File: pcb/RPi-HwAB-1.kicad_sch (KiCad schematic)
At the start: 5 parts, among them U1 CAT24C256

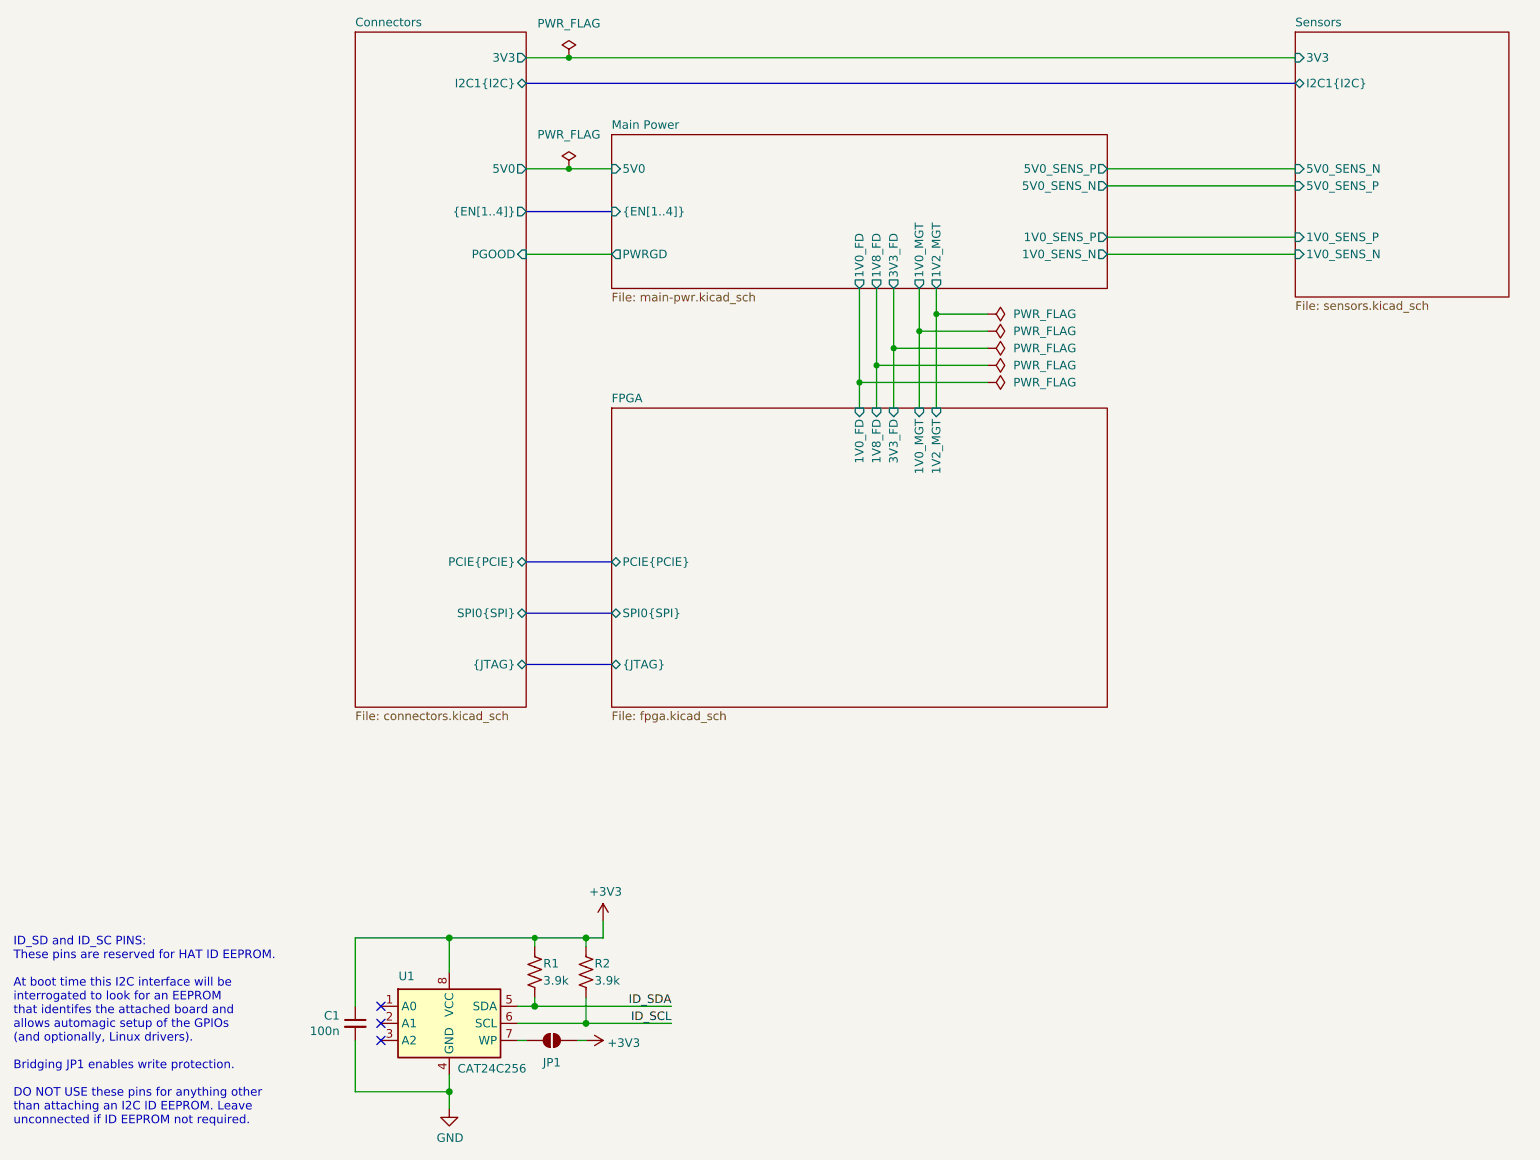
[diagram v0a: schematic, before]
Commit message: added dram, defined pcie sideband sigs.
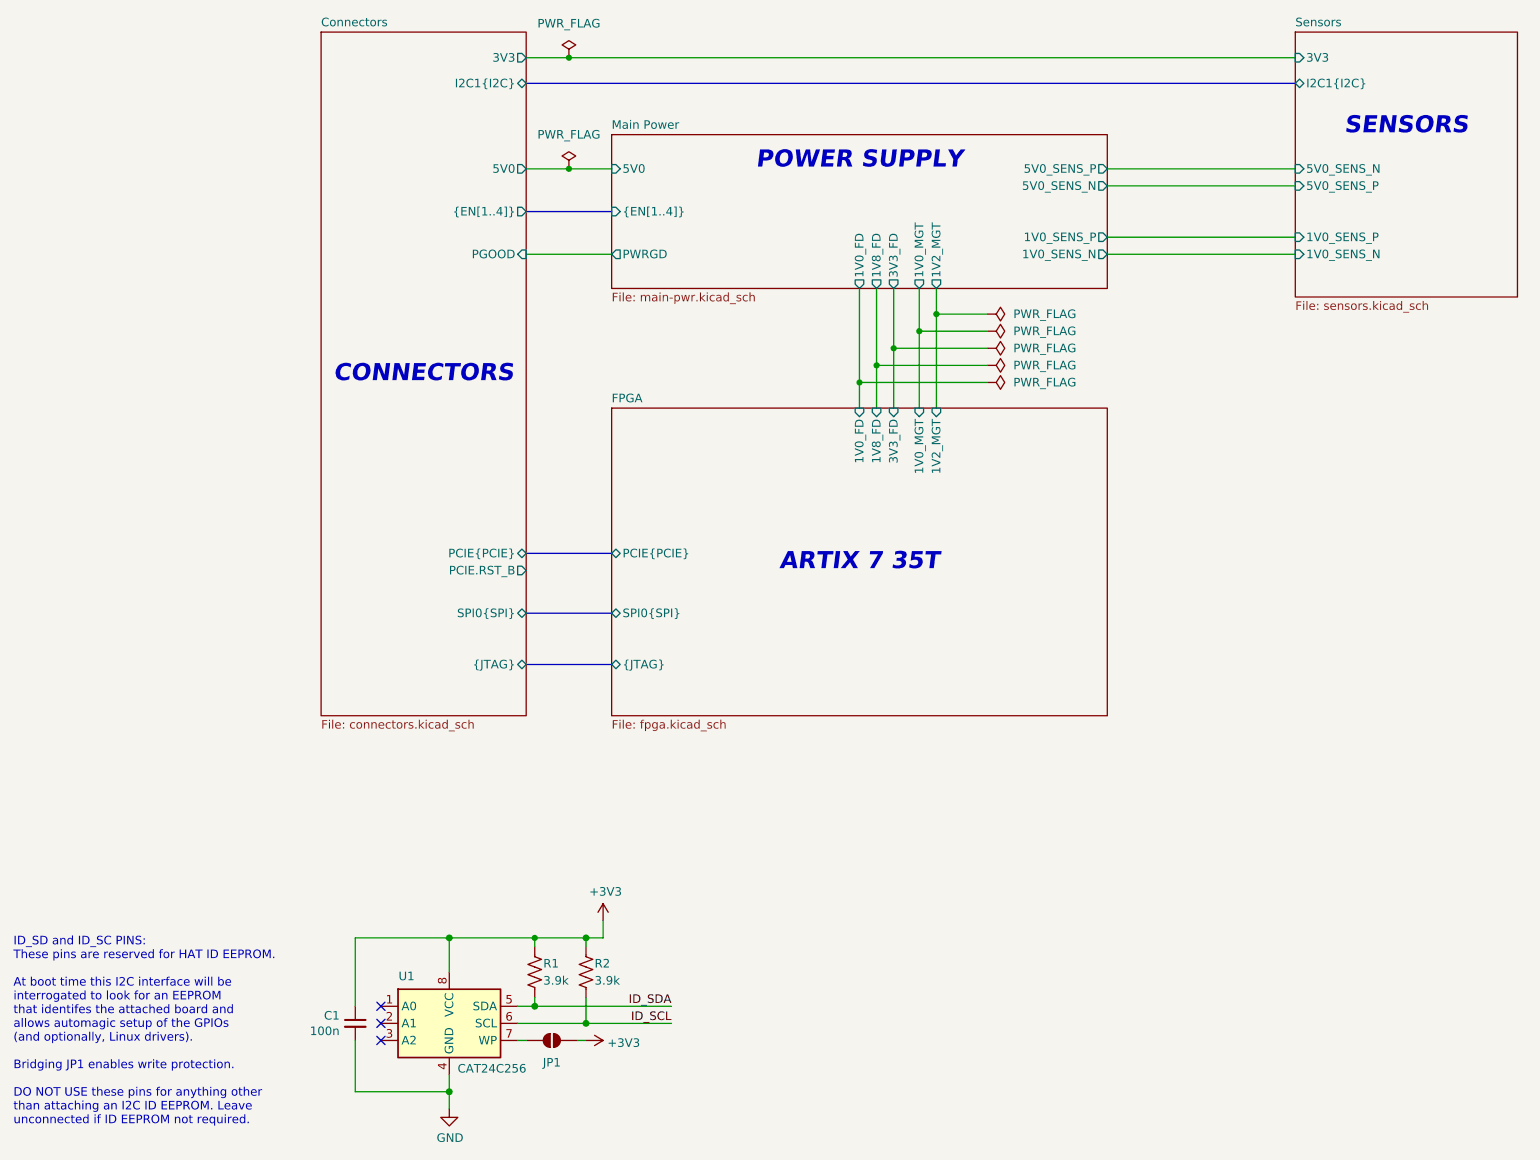
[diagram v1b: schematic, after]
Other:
- sheet Connectors ports: added PCIE.RST_B; removed none
- note added: "ARTIX 7 35T"
- note added: "CONNECTORS"
- note added: "POWER SUPPLY"
- note added: "SENSORS"
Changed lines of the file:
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@@
 		(members "MOSI" "MISO" "SCK" "CS0" "CS1")
+	)
+	(text "ARTIX 7 35T"
+		(exclude_from_sim no)
+		(at 142.24 109.22 0)
+		(effects
+			(font
+				(size 2.54 2.54)
+				(thickness 0.762)
+				(bold yes)
+				(italic yes)
+				(color 0 0 0 1)
+			)
+		)
+	)
+	(text "SENSORS"
+		(exclude_from_sim no)
+		(at 223.52 44.45 0)
+		(effects
+			(font
+				(size 2.54 2.54)
+				(thickness 0.762)
+				(bold yes)
+				(italic yes)
+				(color 0 0 0 1)
+			)
+		)
+	)
+	(text "CONNECTORS"
+		(exclude_from_sim no)
+		(at 77.47 81.28 0)
+		(effects
+			(font
+				(size 2.54 2.54)
+				(thickness 0.762)
+				(bold yes)
+				(italic yes)
+				(color 0 0 0 1)
+			)
+		)
 	)
 	(text "ID_SD and ID_SC PINS:\nThese pins are reserved for HAT ID EEPROM.\n\nAt boot time this I2C interface will be\ninterrogated to look for an EEPROM\nthat identifes the attached board and\nallows automagic setup of the GPIOs\n(and optionally, Linux drivers).\n\nBridging JP1 enables write protection.\n\nDO NOT USE these pins for anything other\nthan attaching an I2C ID EEPROM. Leave\nunconnected if ID EEPROM not required."
@@
 		)
 	)
+	(text "POWER SUPPLY"
+		(exclude_from_sim no)
+		(at 142.24 49.53 0)
+		(effects
+			(font
+				(size 2.54 2.54)
+				(thickness 0.762)
+				(bold yes)
+				(italic yes)
+				(color 0 0 0 1)
+			)
+		)
+	)
 	(junction
 		(at 93.98 175.26)
@@
 	(bus
 		(pts
-			(xy 92.71 109.22) (xy 105.41 109.22)
+			(xy 92.71 107.95) (xy 105.41 107.95)
 		)
 		(stroke
@@
 	(sheet
 		(at 207.01 30.48)
-		(size 31.75 39.37)
+		(size 33.02 39.37)
 		(exclude_from_sim no)
 		(in_bom yes)
@@
 	(sheet
 		(at 105.41 86.36)
-		(size 73.66 44.45)
+		(size 73.66 45.72)
 		(exclude_from_sim no)
 		(in_bom yes)
@@
 		)
 		(property "Sheetfile" "fpga.kicad_sch"
-			(at 105.41 131.3946 0)
+			(at 105.41 132.6646 0)
 			(effects
 				(font
@@
 		)
 		(pin "PCIE{PCIE}" bidirectional
-			(at 105.41 109.22 180)
+			(at 105.41 107.95 180)
 			(effects
 				(font
@@
 	)
 	(sheet
-		(at 67.31 30.48)
-		(size 25.4 100.33)
+		(at 62.23 30.48)
+		(size 30.48 101.6)
 		(exclude_from_sim no)
 		(in_bom yes)
@@
 		)
 		(property "Sheetname" "Connectors"
-			(at 67.31 29.7684 0)
+			(at 62.23 29.7684 0)
 			(effects
 				(font
@@
 		)
 		(property "Sheetfile" "connectors.kicad_sch"
-			(at 67.31 131.3946 0)
+			(at 62.23 132.6646 0)
 			(effects
 				(font
@@
 		)
 		(pin "PCIE{PCIE}" bidirectional
-			(at 92.71 109.22 0)
+			(at 92.71 107.95 0)
 			(effects
 				(font
@@
 			(effects
 				(font
+					(size 1.27 1.27)
+				)
+				(justify right)
+			)
+		)
+		(pin "PCIE.RST_B" output
+			(at 92.71 110.49 0)
+			(effects
+				(font

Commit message: added potential power sequencer
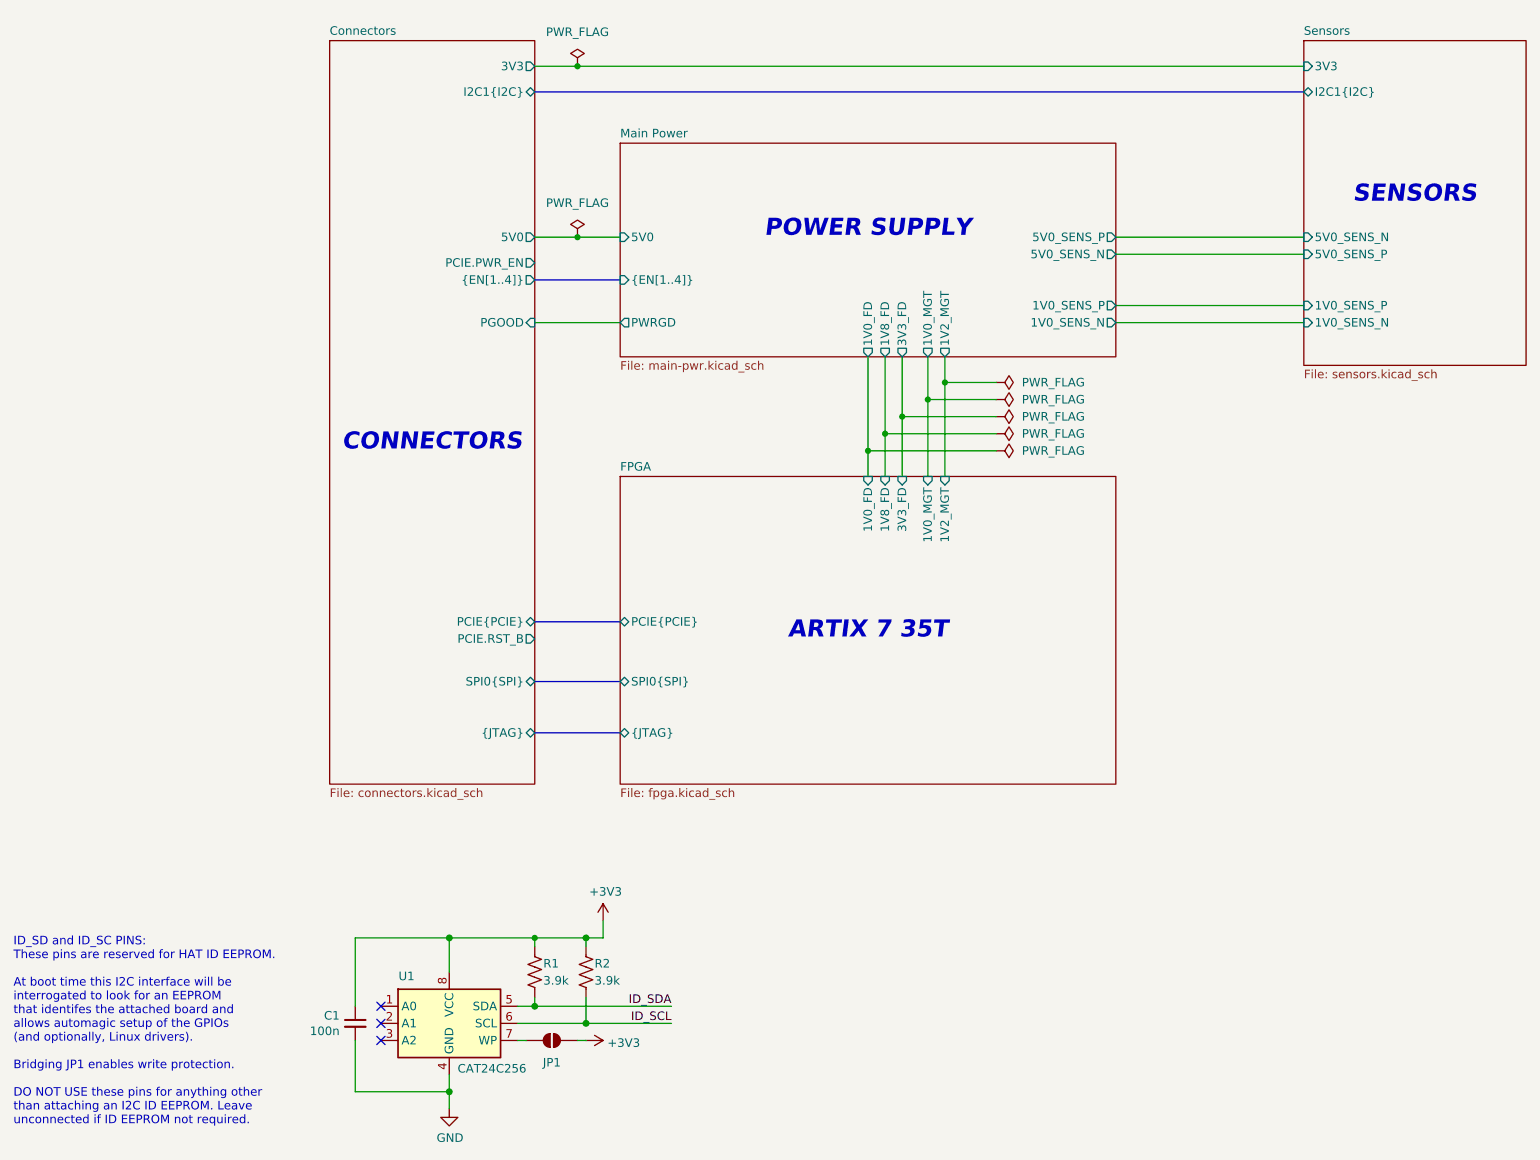
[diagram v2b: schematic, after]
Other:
- sheet Connectors ports: added PCIE.PWR_EN; removed none

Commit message: saved libraries to project
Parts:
- C1: symbol Device:C_Small -> library:C_Small
- JP1: symbol Jumper:SolderJumper_2_Open -> library:SolderJumper_2_Open
- R1, R2: symbol Device:R_US -> library:R_US
- U1: symbol Memory_EEPROM:CAT24C256 -> library:CAT24C256
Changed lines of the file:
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@@
 	)
 	(symbol
-		(lib_id "Device:R_US")
+		(lib_id "library:R_US")
 		(at 93.98 170.18 0)
 		(unit 1)
@@
 	)
 	(symbol
-		(lib_id "Device:C_Small")
+		(lib_id "library:C_Small")
 		(at 67.31 177.8 0)
 		(unit 1)
@@
 	)
 	(symbol
-		(lib_id "Jumper:SolderJumper_2_Open")
+		(lib_id "library:SolderJumper_2_Open")
 		(at 96.52 180.34 0)
 		(unit 1)
@@
 	)
 	(symbol
-		(lib_id "power:+3.3V")
+		(lib_id "library:+3.3V")
 		(at 104.14 162.56 0)
 		(unit 1)
@@
 	)
 	(symbol
-		(lib_id "power:PWR_FLAG")
+		(lib_id "library:PWR_FLAG")
 		(at 162.56 87.63 270)
 		(unit 1)
@@
 	)
 	(symbol
-		(lib_id "power:PWR_FLAG")
+		(lib_id "library:PWR_FLAG")
 		(at 162.56 85.09 270)
 		(unit 1)
@@
 	)
 	(symbol
-		(lib_id "power:PWR_FLAG")
+		(lib_id "library:PWR_FLAG")
 		(at 162.56 90.17 270)
 		(unit 1)
@@
 	)
 	(symbol
-		(lib_id "Memory_EEPROM:CAT24C256")
+		(lib_id "library:CAT24C256")
 		(at 81.28 177.8 0)
 		(unit 1)
@@
 	)
 	(symbol
-		(lib_id "power:PWR_FLAG")
+		(lib_id "library:PWR_FLAG")
 		(at 100.33 35.56 0)
 		(unit 1)
@@
 	)
 	(symbol
-		(lib_id "power:GND")
+		(lib_id "library:GND")
 		(at 81.28 190.5 0)
 		(unit 1)
@@
 	)
 	(symbol
-		(lib_id "power:+3.3V")
+		(lib_id "library:+3.3V")
 		(at 101.6 180.34 270)
 		(unit 1)
@@
 	)
 	(symbol
-		(lib_id "Device:R_US")
+		(lib_id "library:R_US")
 		(at 101.6 170.18 0)
 		(unit 1)
@@
 	)
 	(symbol
-		(lib_id "power:PWR_FLAG")
+		(lib_id "library:PWR_FLAG")
 		(at 162.56 82.55 270)
 		(unit 1)
@@
 	)
 	(symbol
-		(lib_id "power:PWR_FLAG")
+		(lib_id "library:PWR_FLAG")
 		(at 162.56 92.71 270)
 		(unit 1)
@@
 	)
 	(symbol
-		(lib_id "power:PWR_FLAG")
+		(lib_id "library:PWR_FLAG")
 		(at 100.33 60.96 0)
 		(unit 1)

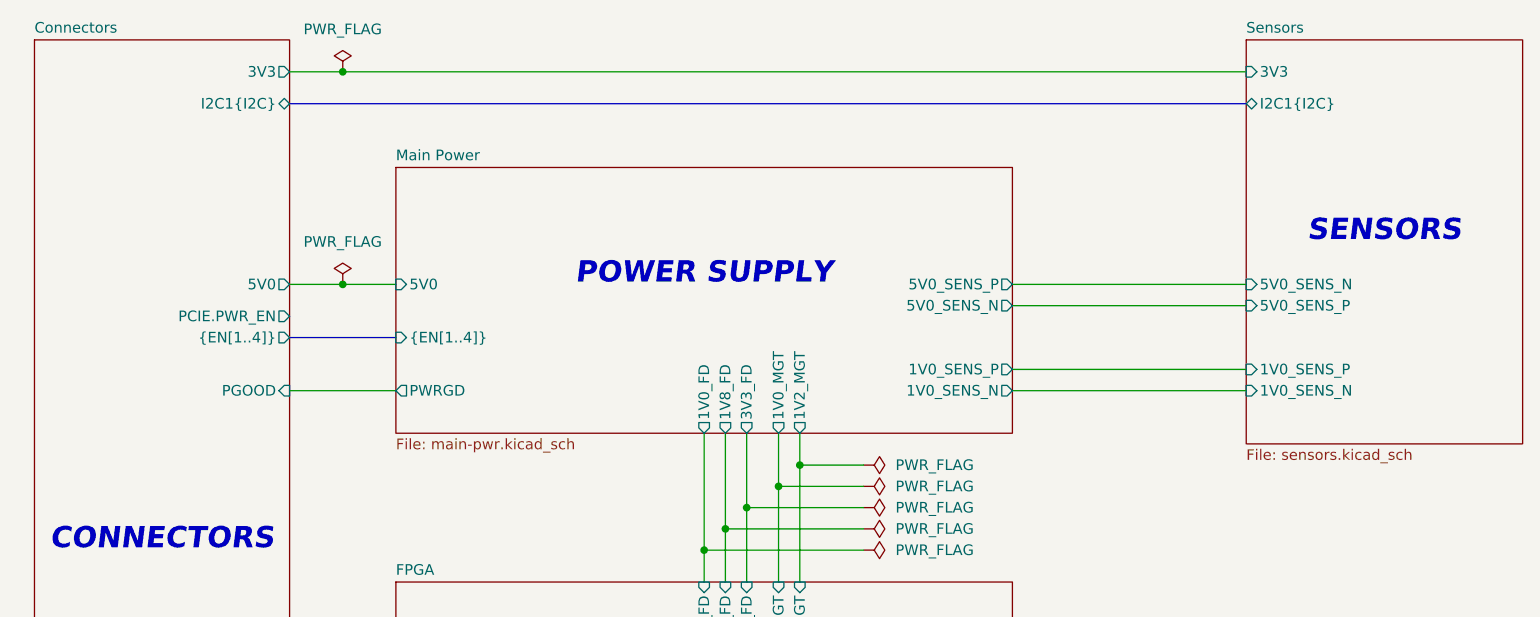
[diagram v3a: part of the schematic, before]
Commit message: hierarchy and power sequencing, level shift
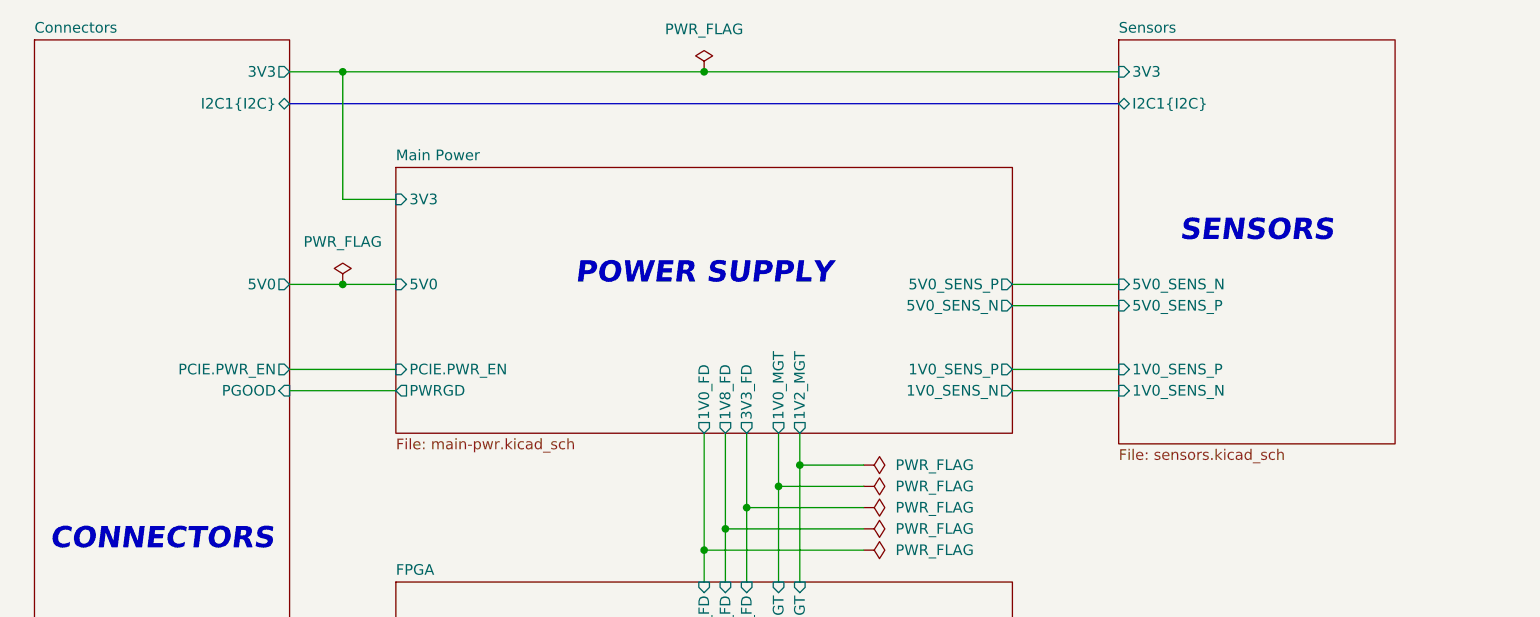
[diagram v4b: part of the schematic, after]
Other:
- sheet Connectors ports: added none; removed {EN[1..4]}
- sheet Main Power ports: added 3V3, PCIE.PWR_EN; removed {EN[1..4]}

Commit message: added hierarchical sheet, pwr seq
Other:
- sheet FPGA ports: added PCIE.RST_B; removed none
